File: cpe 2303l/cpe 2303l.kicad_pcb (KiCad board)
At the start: 2 copper layers, 3 parts

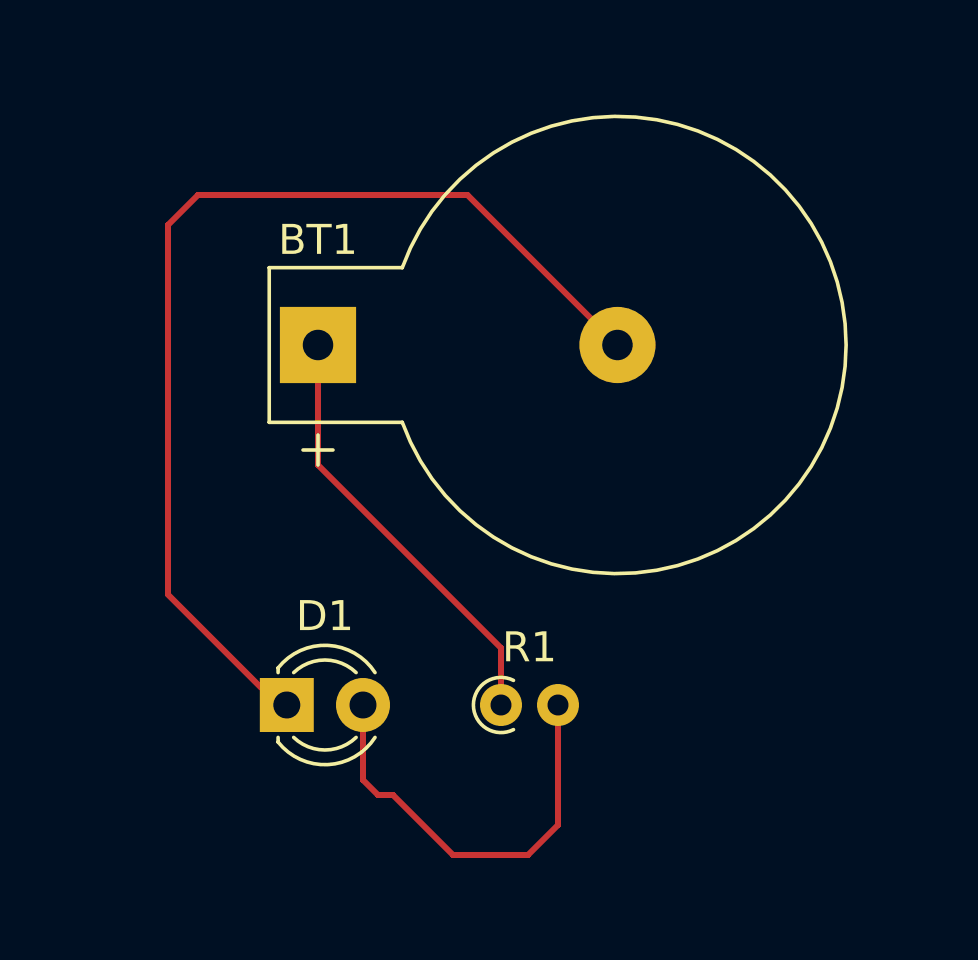
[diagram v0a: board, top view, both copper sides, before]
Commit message: Add initial KiCad project files for Arduino Nano module
- Created a new KiCad project file (test.kicad_pro) with board design settings, including default rules and dimensions.
- Added schematic file (test.kicad_sch) for Arduino Nano module, including symbol definitions, properties, and pin configurations.
- Included metadata for versioning and library references.
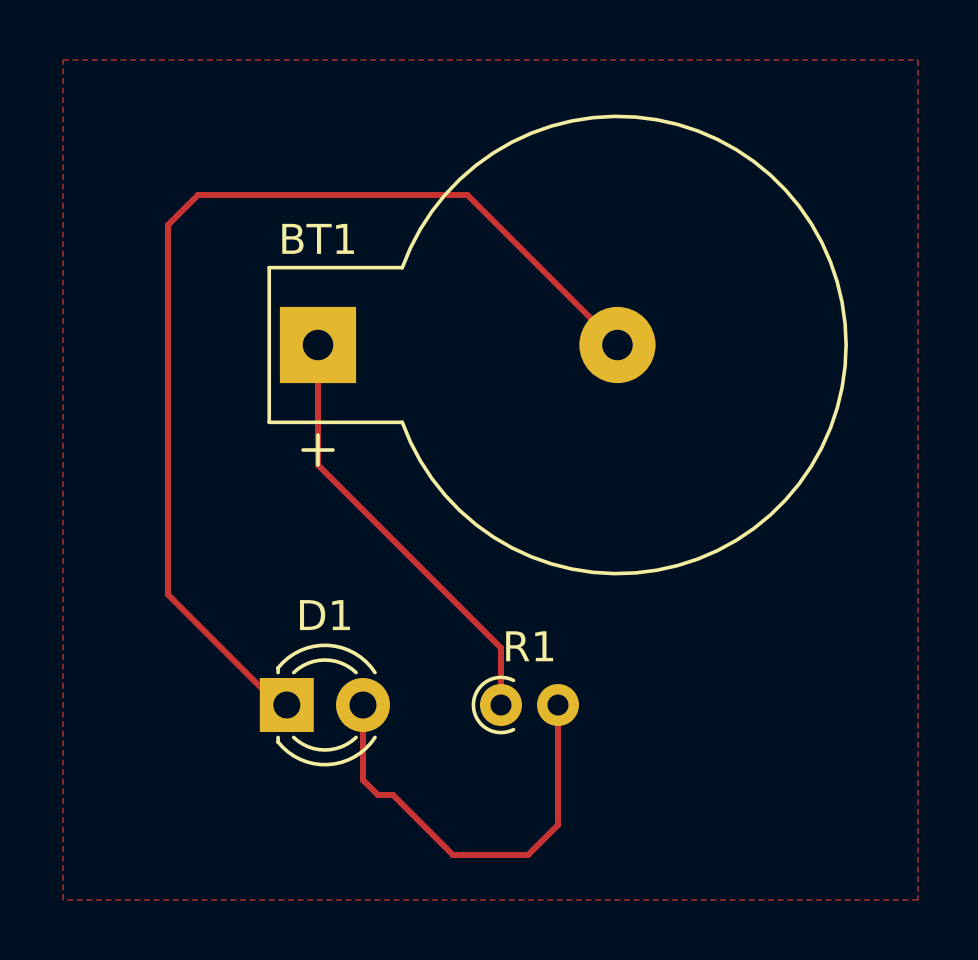
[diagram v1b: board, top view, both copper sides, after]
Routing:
- added copper zone on F.Cu, net Net-(BT1-+)
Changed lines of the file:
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@@
 		(net 3)
+	)
+	(zone
+		(net 2)
+		(net_name "Net-(BT1-+)")
+		(layer "F.Cu")
+		(hatch edge 0.5)
+		(connect_pads
+			(clearance 0.5)
+		)
+		(min_thickness 0.25)
+		(filled_areas_thickness no)
+		(fill
+			(thermal_gap 0.5)
+			(thermal_bridge_width 0.5)
+		)
+		(polygon
+			(pts
+				(xy 100 72.5) (xy 128.5 72.5) (xy 128.5 100.5) (xy 100 100.5)
+			)
+		)
 	)
 	(embedded_fonts no)

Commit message: Refactor code structure for improved readability and maintainability
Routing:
- net Net-(BT1--): track 34.9 -> 40.6 mm
- net Net-(D1-A): track 14.4 -> 11.7 mm
- removed copper zone on F.Cu, net Net-(BT1-+)
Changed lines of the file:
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@@
 		)
+	)
+	(gr_rect
+		(start 100 73.5)
+		(end 127.5 100)
+		(stroke
+			(width 0.2)
+			(type default)
+		)
+		(fill no)
+		(layer "F.Cu")
+	)
+	(segment
+		(start 104.5 76)
+		(end 103.5 77)
+		(width 0.2)
+		(layer "B.Cu")
+		(net 1)
+	)
+	(segment
+		(start 103.5 77)
+		(end 103.5 93)
+		(width 0.2)
+		(layer "B.Cu")
+		(net 1)
 	)
 	(segment
 		(start 118.4822 82)
-		(end 113.4822 77)
+		(end 118.4822 77.9822)
 		(width 0.2)
-		(layer "F.Cu")
+		(layer "B.Cu")
 		(net 1)
 	)
 	(segment
-		(start 106.84 93.66)
-		(end 106.81 93.66)
+		(start 118.4822 77.9822)
+		(end 116.5 76)
 		(width 0.2)
-		(layer "F.Cu")
+		(layer "B.Cu")
 		(net 1)
 	)
 	(segment
-		(start 113.4822 77)
-		(end 104.5 77)
+		(start 116.5 76)
+		(end 104.5 76)
 		(width 0.2)
-		(layer "F.Cu")
+		(layer "B.Cu")
 		(net 1)
 	)
 	(segment
-		(start 103.5 90.32)
-		(end 106.68 93.5)
+		(start 103.5 93)
+		(end 104.5 94)
 		(width 0.2)
-		(layer "F.Cu")
+		(layer "B.Cu")
 		(net 1)
 	)
 	(segment
-		(start 104.5 77)
-		(end 103.5 78)
+		(start 104.5 94)
+		(end 107.46 94)
 		(width 0.2)
-		(layer "F.Cu")
+		(layer "B.Cu")
 		(net 1)
 	)
 	(segment
-		(start 106.68 93.5)
-		(end 107 93.5)
+		(start 114.6 94)
+		(end 108.5 87.9)
 		(width 0.2)
-		(layer "F.Cu")
-		(net 1)
-	)
-	(segment
-		(start 103.5 78)
-		(end 103.5 90.32)
-		(width 0.2)
-		(layer "F.Cu")
-		(net 1)
-	)
-	(segment
-		(start 107 93.5)
-		(end 106.84 93.66)
-		(width 0.2)
-		(layer "F.Cu")
-		(net 1)
-	)
-	(segment
-		(start 114.6 92.1)
-		(end 114.6 94)
-		(width 0.2)
-		(layer "F.Cu")
+		(layer "B.Cu")
 		(net 2)
 	)
 	(segment
-		(start 108.5 86)
-		(end 114.6 92.1)
+		(start 108.5 87.9)
+		(end 108.5 82)
 		(width 0.2)
-		(layer "F.Cu")
+		(layer "B.Cu")
 		(net 2)
 	)
 	(segment
-		(start 108.5 82)
-		(end 108.5 86)
+		(start 110 95.5)
+		(end 112 97.5)
 		(width 0.2)
-		(layer "F.Cu")
-		(net 2)
-	)
-	(segment
-		(start 116.5 94)
-		(end 116.5 98)
-		(width 0.2)
-		(layer "F.Cu")
+		(layer "B.Cu")
 		(net 3)
 	)
 	(segment
-		(start 110.5 97)
-		(end 110 96.5)
+		(start 112 97.5)
+		(end 115.5 97.5)
 		(width 0.2)
-		(layer "F.Cu")
+		(layer "B.Cu")
 		(net 3)
 	)
 	(segment
-		(start 111 97)
-		(end 110.5 97)
+		(start 110 94)
+		(end 110 95.5)
 		(width 0.2)
-		(layer "F.Cu")
+		(layer "B.Cu")
 		(net 3)
 	)
 	(segment
-		(start 116.5 98)
-		(end 115.5 99)
+		(start 116.5 96.5)
+		(end 116.5 94)
 		(width 0.2)
-		(layer "F.Cu")
+		(layer "B.Cu")
 		(net 3)
 	)
 	(segment
-		(start 113 99)
-		(end 111 97)
+		(start 115.5 97.5)
+		(end 116.5 96.5)
 		(width 0.2)
-		(layer "F.Cu")
+		(layer "B.Cu")
 		(net 3)
 	)
-	(segment
-		(start 115.5 99)
-		(end 113 99)
-		(width 0.2)
-		(layer "F.Cu")
-		(net 3)
-	)
-	(segment
-		(start 110 96.5)
-		(end 110 94)
-		(width 0.2)
-		(layer "F.Cu")
-		(net 3)
-	)
-	(zone
-		(net 2)
-		(net_name "Net-(BT1-+)")
-		(layer "F.Cu")
-		(hatch edge 0.5)
-		(connect_pads
-			(clearance 0.5)
-		)
-		(min_thickness 0.25)
-		(filled_areas_thickness no)
-		(fill
-			(thermal_gap 0.5)
-			(thermal_bridge_width 0.5)
-		)
-		(polygon
-			(pts
-				(xy 100 72.5) (xy 128.5 72.5) (xy 128.5 100.5) (xy 100 100.5)
-			)
-		)
-	)
 	(embedded_fonts no)

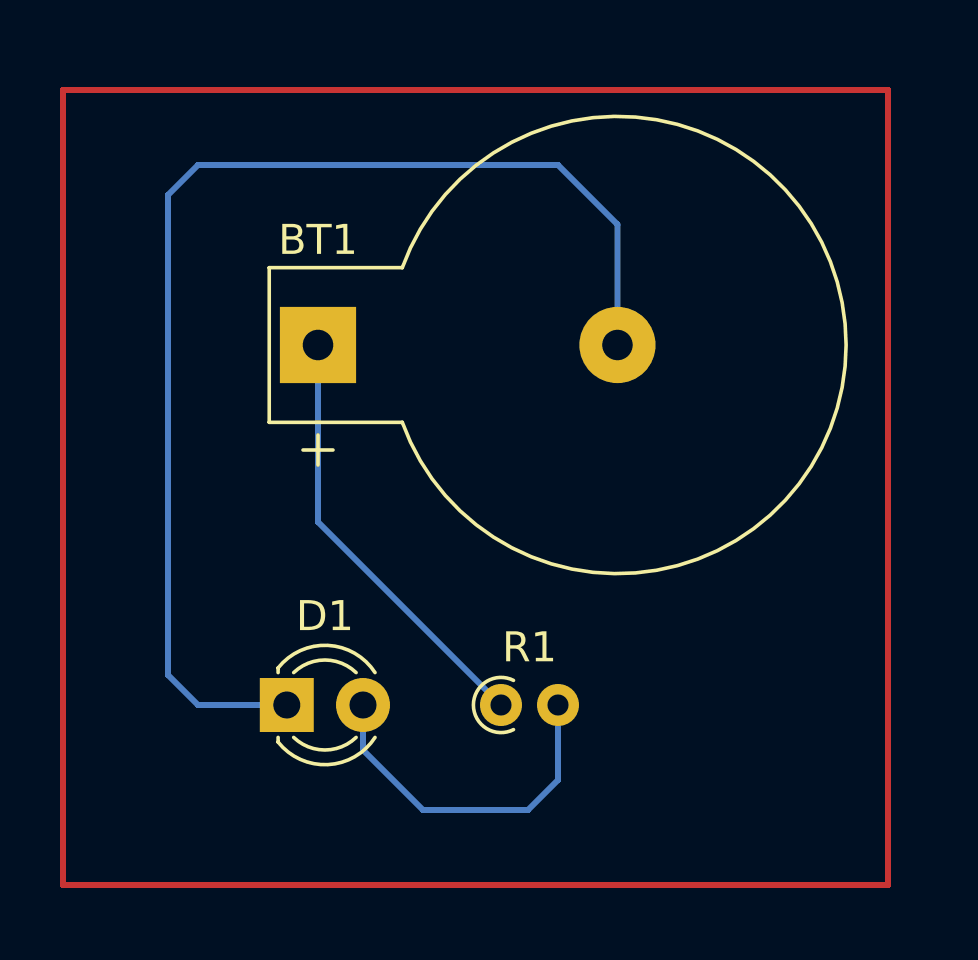
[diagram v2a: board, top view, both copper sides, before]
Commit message: Add lock file for KiCad PCB project with hostname and username
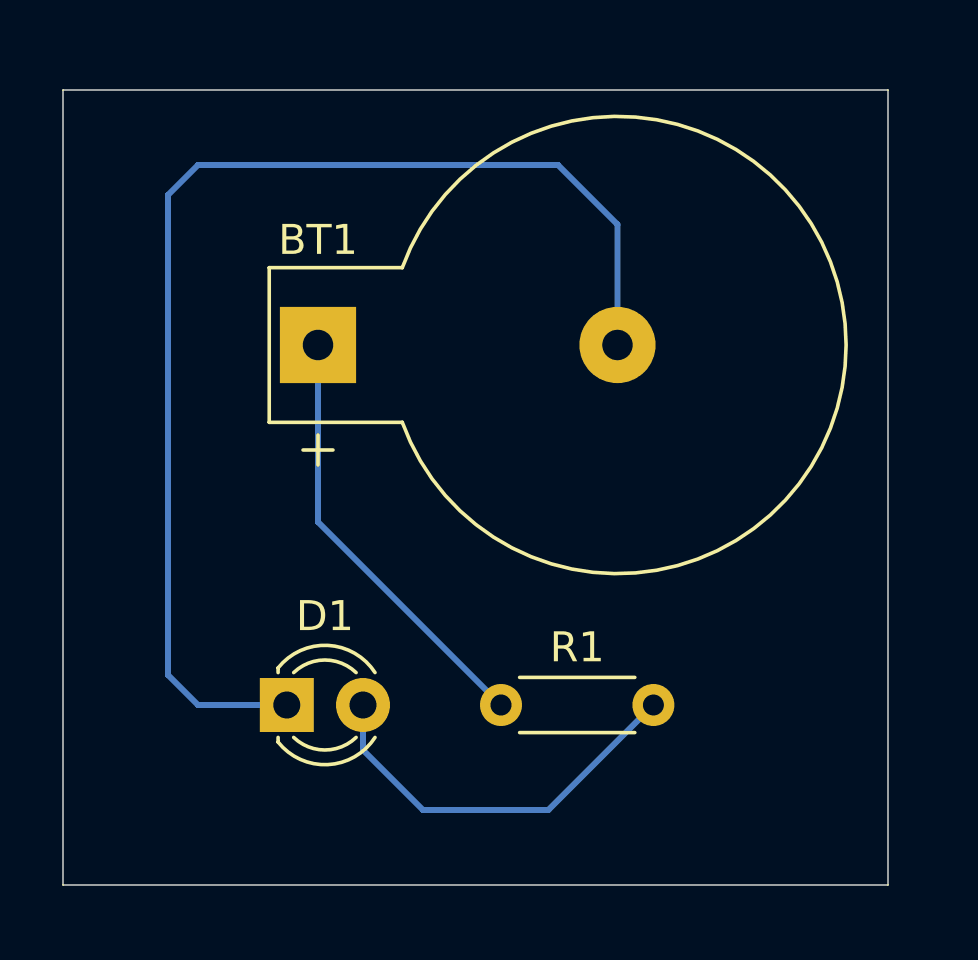
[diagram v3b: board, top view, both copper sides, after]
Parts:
- R1: footprint Resistor_THT:R_Axial_DIN0204_L3.6mm_D1.6mm_P1.90mm_Vertical -> Resistor_THT:R_Axial_DIN0204_L3.6mm_D1.6mm_P5.08mm_Horizontal
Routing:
- net Net-(D1-A): track 11.7 -> 13.5 mm
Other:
- board outline added: 27.5 x 26.5 mm
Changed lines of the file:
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@@
 		)
 	)
-	(footprint "Resistor_THT:R_Axial_DIN0204_L3.6mm_D1.6mm_P1.90mm_Vertical"
+	(footprint "Resistor_THT:R_Axial_DIN0204_L3.6mm_D1.6mm_P5.08mm_Horizontal"
 		(layer "F.Cu")
 		(at 114.6 94)
-		(descr "Resistor, Axial_DIN0204 series, Axial, Vertical, pin pitch=1.9mm, 0.167W, length*diameter=3.6*1.6mm^2, http://cdn-reichelt.de/documents/datenblatt/B400/1_4W%23YAG.pdf")
-		(tags "Resistor Axial_DIN0204 series Axial Vertical pin pitch 1.9mm 0.167W length 3.6mm diameter 1.6mm")
+		(descr "Resistor, Axial_DIN0204 series, Axial, Horizontal, pin pitch=5.08mm, 0.167W, length*diameter=3.6*1.6mm^2, http://cdn-reichelt.de/documents/datenblatt/B400/1_4W%23YAG.pdf")
+		(tags "Resistor Axial_DIN0204 series Axial Horizontal pin pitch 5.08mm 0.167W length 3.6mm diameter 1.6mm")
 		(property "Reference" "R1"
-			(at 0.95 -1.92 0)
+			(at 2.54 -1.92 0)
 			(layer "F.SilkS")
 			(effects
@@
 		)
 		(property "Value" "100"
-			(at 0.95 1.92 0)
+			(at 2.54 1.92 0)
 			(layer "F.Fab")
 			(effects
@@
 			)
 		)
-		(property "Description" "Resistor"
+		(property "Description" ""
 			(at 0 0 0)
 			(layer "F.Fab")
@@
 		(sheetfile "cpe 2303l.kicad_sch")
 		(attr through_hole)
-		(fp_arc
-			(start 0.417133 0.82)
-			(mid -0.92 0)
-			(end 0.417133 -0.82)
+		(fp_line
+			(start 0.62 -0.92)
+			(end 4.46 -0.92)
 			(stroke
 				(width 0.12)
@@
 			(layer "F.SilkS")
 		)
+		(fp_line
+			(start 0.62 0.92)
+			(end 4.46 0.92)
+			(stroke
+				(width 0.12)
+				(type solid)
+			)
+			(layer "F.SilkS")
+		)
 		(fp_rect
-			(start -1.05 -1.05)
-			(end 2.86 1.05)
+			(start -0.95 -1.05)
+			(end 6.03 1.05)
 			(stroke
 				(width 0.05)
@@
 		(fp_line
 			(start 0 0)
-			(end 1.9 0)
+			(end 0.74 0)
 			(stroke
 				(width 0.1)
@@
 			(layer "F.Fab")
 		)
-		(fp_circle
-			(center 0 0)
-			(end 0.8 0)
+		(fp_line
+			(start 5.08 0)
+			(end 4.34 0)
 			(stroke
 				(width 0.1)
 				(type solid)
 			)
+			(layer "F.Fab")
+		)
+		(fp_rect
+			(start 0.74 -0.8)
+			(end 4.34 0.8)
+			(stroke
+				(width 0.1)
+				(type solid)
+			)
 			(fill no)
 			(layer "F.Fab")
 		)
 		(fp_text user "${REFERENCE}"
-			(at 0.95 -1.92 0)
-			(layer "F.Fab")
-			(effects
-				(font
-					(size 1 1)
-					(thickness 0.15)
+			(at 2.54 0 0)
+			(layer "F.Fab")
+			(effects
+				(font
+					(size 0.72 0.72)
+					(thickness 0.108)
 				)
 			)
@@
 		)
 		(pad "2" thru_hole circle
-			(at 1.9 0)
+			(at 5.08 0)
 			(size 1.4 1.4)
 			(drill 0.7)
@@
 		)
 		(embedded_fonts no)
-		(model "${KICAD9_3DMODEL_DIR}/Resistor_THT.3dshapes/R_Axial_DIN0204_L3.6mm_D1.6mm_P1.90mm_Vertical.step"
+		(model "${KICAD9_3DMODEL_DIR}/Resistor_THT.3dshapes/R_Axial_DIN0204_L3.6mm_D1.6mm_P5.08mm_Horizontal.step"
 			(offset
 				(xyz 0 0 0)
@@
 		(end 127.5 100)
 		(stroke
-			(width 0.2)
+			(width 0.05)
 			(type default)
 		)
 		(fill no)
-		(layer "F.Cu")
+		(layer "Edge.Cuts")
 	)
 	(segment
@@
 	)
 	(segment
-		(start 112 97.5)
-		(end 115.5 97.5)
-		(width 0.2)
-		(layer "B.Cu")
-		(net 3)
-	)
-	(segment
 		(start 110 94)
 		(end 110 95.5)
@@
 	)
 	(segment
-		(start 116.5 96.5)
-		(end 116.5 94)
+		(start 119.68 94)
+		(end 116.18 97.5)
 		(width 0.2)
 		(layer "B.Cu")
@@
 	)
 	(segment
-		(start 115.5 97.5)
-		(end 116.5 96.5)
-		(width 0.2)
-		(layer "B.Cu")
+		(start 116.18 97.5)
+		(end 112 97.5)
+		(width 0.2)
+		(layer "B.Cu")
